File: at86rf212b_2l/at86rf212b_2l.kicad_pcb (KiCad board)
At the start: 2 copper layers, 35 x 24.9 mm, 23 parts, among them J1 ANT, J2 Conn_01x07, J3 Conn_01x07, U1 AT86RF212B, Y1 16.0Mhz

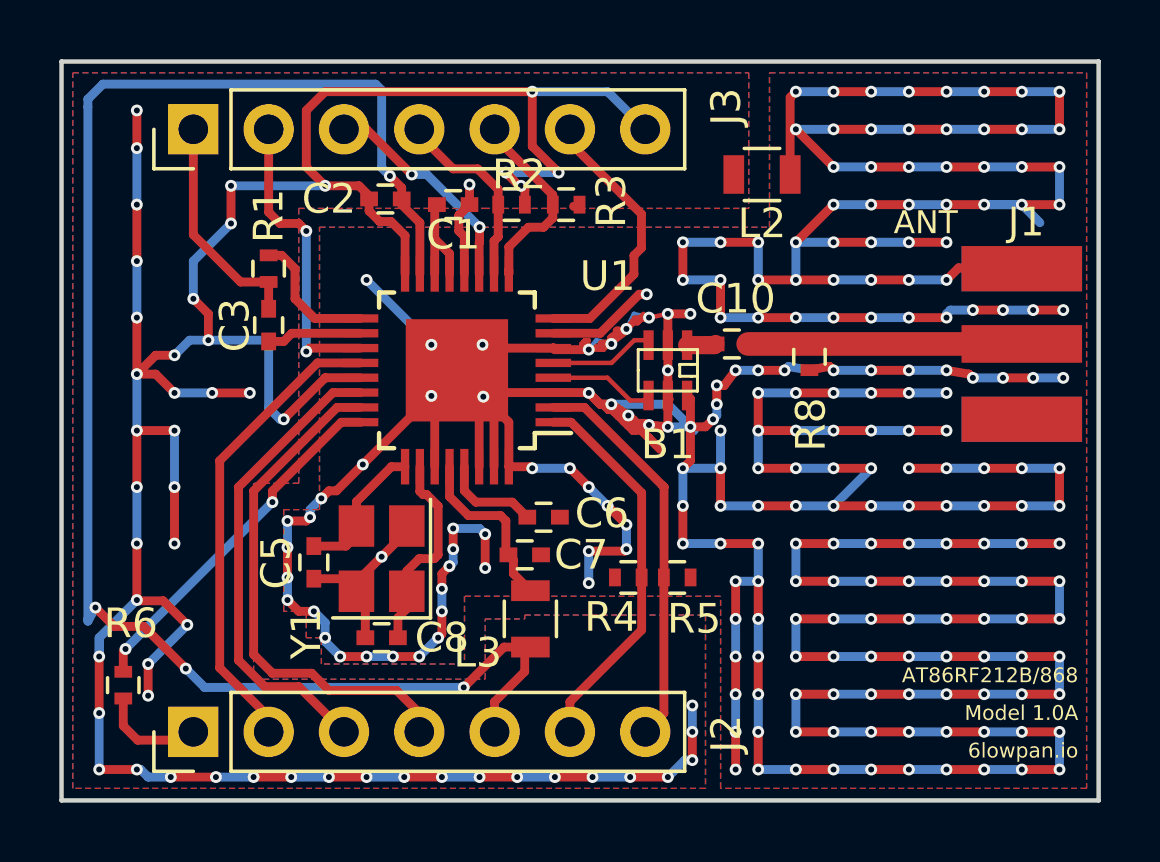
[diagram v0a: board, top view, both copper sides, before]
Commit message: Latest commits. Splitting ground planes in 4: Digital, Analog, Xtal & RF. All 4 connected in the QFN package, essentially following a "star" formation. Spacing is around 12 mils, so most fabs can handle it on a 35um copper 2 layer board. Not the most beautiful design, as it was cut and stitch, but should be OK.
Also latest Gerber plots in the plots directory.
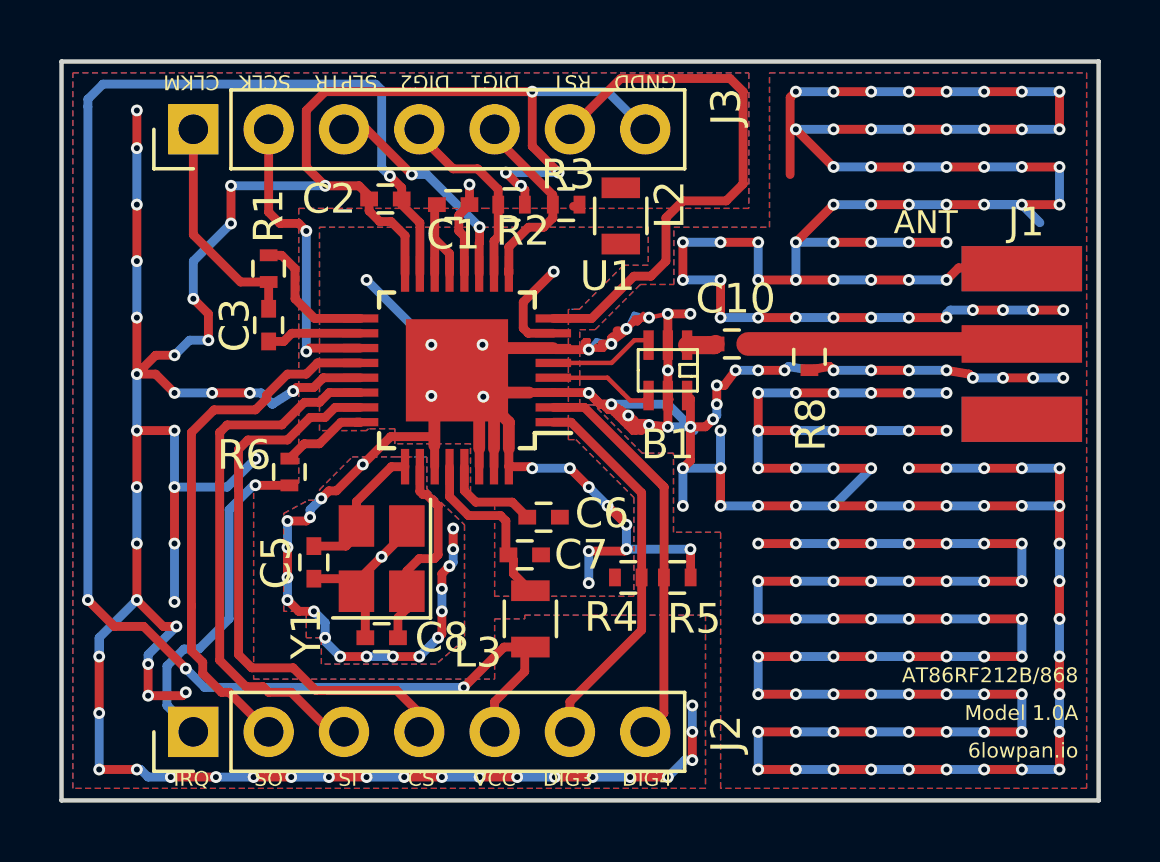
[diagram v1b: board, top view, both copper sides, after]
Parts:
- moved R6 9.11 mm to (178.5, 85.2)
- moved L2 4.96 mm to (189.7, 76.6), turned to 90 degrees
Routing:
- net /RST: track 9.33 -> 19.0 mm
- net /IRQ: track 3.60 -> 12.7 mm, vias 0 -> 1
- net Net-(R6-Pad1): track 12.1 -> 3.06 mm, vias 2 -> 0
- net GND: track 326.4 -> 318.2 mm, vias 226 -> 217
- net /CS: track 17.3 -> 21.5 mm
- net /MOSI: track 15.8 -> 18.2 mm
- net /MISO: track 15.9 -> 18.1 mm
- net GNDPWR: track 112.7 -> 114.6 mm, vias 52 -> 55
- net VCC: track 54.5 -> 53.6 mm
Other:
- board text added: "CLKM"
- board text added: "CS"
- board text added: "DIG1"
- board text added: "DIG2"
- board text added: "DIG3"
- board text added: "DIG4"
- board text added: "GNDD"
- board text added: "IRQ"
- board text added: "RST"
- board text added: "SCLK"
- board text added: "SI"
- board text added: "SLPTR"
- board text added: "SO"
- board text added: "VCC"

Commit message: AT86RFR212b package, mistakenly used QFP instaed of the proper QFN 32 bit package. Now fixed. That lead to some minor tweaks and fixes around the ground planes. Also moved the resistor for the IRQ, everything else is the same. Tracks are reduced to 0.2mm, as our manufacturing company is producing those without a problem and we also have 0.1mm tracks for the antenna feed lines, so there is no change of price. Also tweaked the pad design rules for the solder paste mask. You will see the plots. Missing is the SVG for the mask, but that will come later. Components are here, BOM to follow shortly.
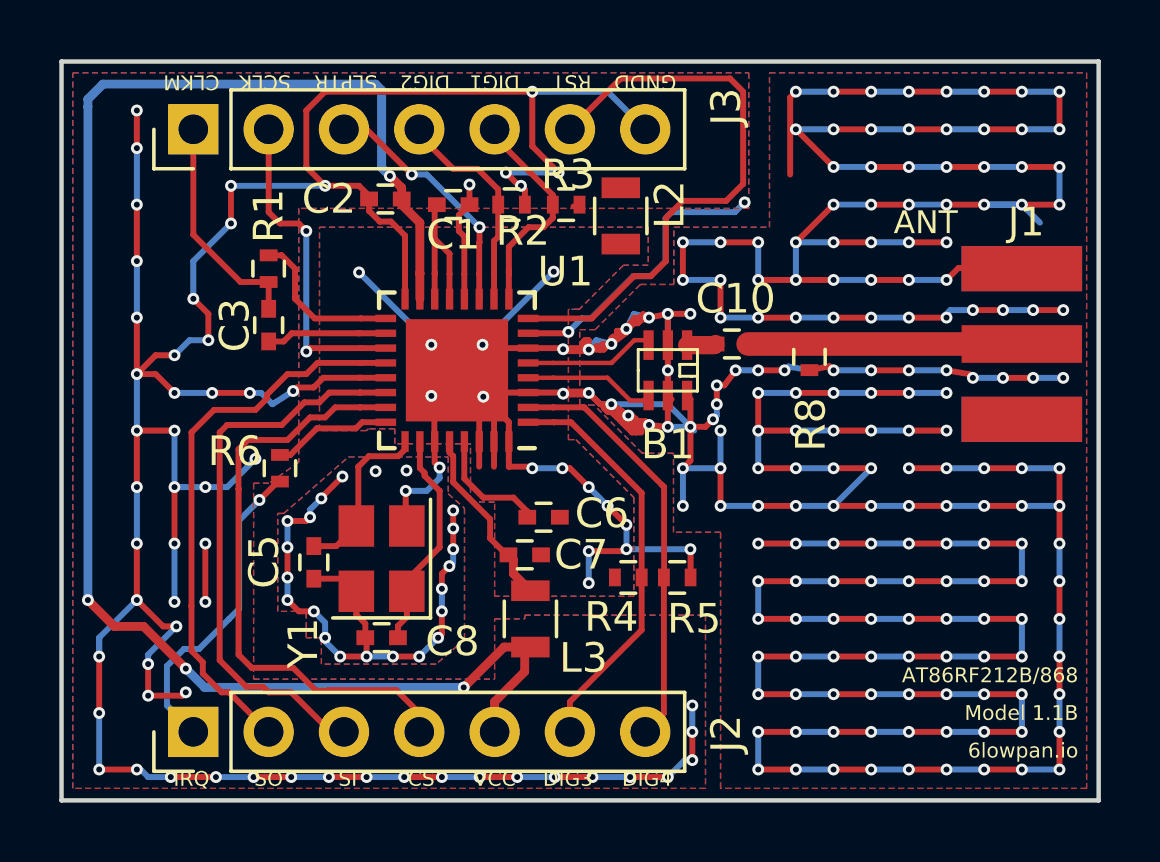
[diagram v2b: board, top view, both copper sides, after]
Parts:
- U1: footprint Housings_QFP:LQFP-32-1EP_5x5mm_Pitch0.5mm -> Housings_DFN_QFN:QFN-32-1EP_5x5mm_Pitch0.5mm
- moved R6 0.34 mm to (178.2, 85.1)
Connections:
- U1 pad 7: GND -> GNDPWR
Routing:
- net GNDPWR: track 114.6 -> 130.5 mm, vias 55 -> 60
- net Net-(C10-Pad1): track 9.91 -> 12.0 mm
- net Net-(C1-Pad1): track 3.76 -> 5.48 mm
- net GND: track 318.2 -> 316.7 mm, vias 217 -> 223
- net Net-(C5-Pad2): track 4.85 -> 5.83 mm
- net Net-(R6-Pad1): track 3.06 -> 4.03 mm
- net VCC: track 53.6 -> 54.5 mm
- net /MOSI: track 18.2 -> 19.1 mm
- net /DIG3: track 13.2 -> 14.1 mm
- net /CS: track 21.5 -> 22.3 mm
- net /SLPTR: track 7.52 -> 8.37 mm
- net /MISO: track 18.1 -> 18.9 mm
- net /DIG2: track 6.52 -> 7.37 mm
- net /DIG1: track 6.75 -> 7.61 mm
- net /DIG4: track 13.4 -> 14.2 mm
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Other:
- board text added: "Model 1.1B"
- board text removed: "Model 1.0A"
